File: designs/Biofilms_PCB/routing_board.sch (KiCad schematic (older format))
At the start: 11 parts

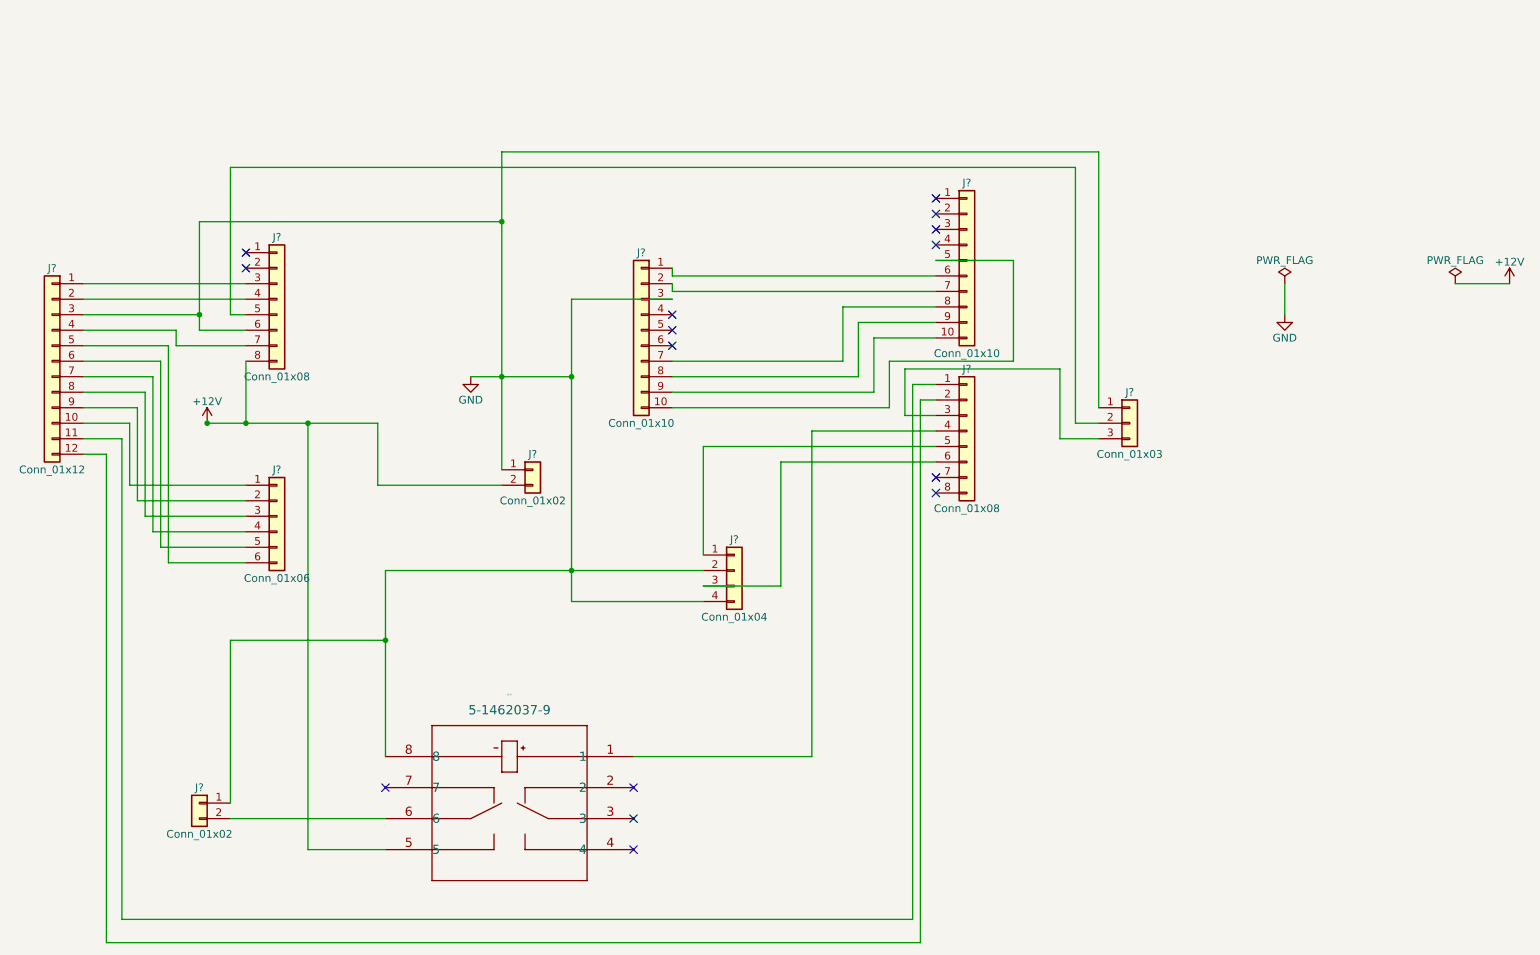
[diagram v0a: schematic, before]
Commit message: drafted v1 of biofilms PCB
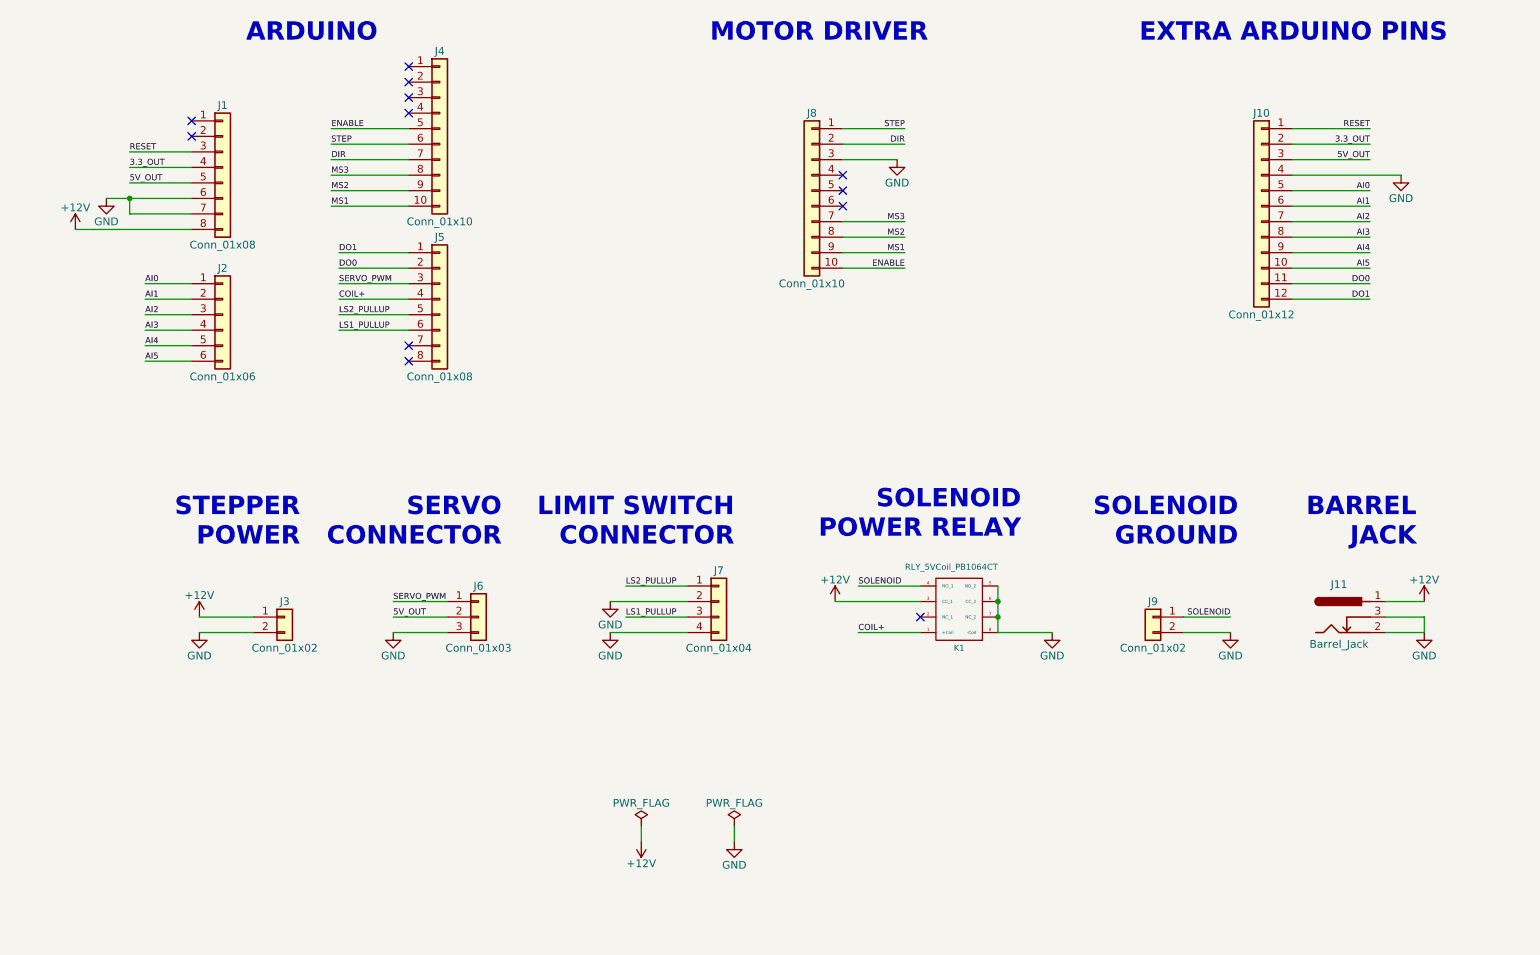
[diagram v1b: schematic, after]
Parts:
- removed RLY?: 5-1462037-9, 5-1462037-9, symbol 5-1462037-9
- added J11: Barrel_Jack, Connectors:BARREL_JACK, symbol Barrel_Jack
- added K1: RLY_5VCoil_PB1064CT, Relays_THT:Relay_DPDT_AXICOM_IMSeries_Pitch3.2mm, symbol RLY_5VCoil_PB1064CT
- J1, J5: renamed from J?; footprint (none) -> Pin_Headers:Pin_Header_Straight_1x08_Pitch2.54mm
- J10: renamed from J?; footprint (none) -> Socket_Strips:Socket_Strip_Straight_1x12_Pitch2.54mm
- J2: renamed from J?; footprint (none) -> Pin_Headers:Pin_Header_Straight_1x06_Pitch2.54mm
- J3, J9: renamed from J?; footprint (none) -> Socket_Strips:Socket_Strip_Straight_1x02_Pitch2.54mm
- J4, J8: renamed from J?; footprint (none) -> Pin_Headers:Pin_Header_Straight_1x10_Pitch2.54mm
- J6: renamed from J?; footprint (none) -> Pin_Headers:Pin_Header_Straight_1x03_Pitch2.54mm
- J7: renamed from J?; footprint (none) -> Socket_Strips:Socket_Strip_Straight_1x04_Pitch2.54mm
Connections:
- net +12V: now also J3.1 (Pin_1), J11.1, K1.3 (CC_1); no longer J3.2 (Pin_2)
- net GND: now also J1.7 (Pin_7), J10.4 (Pin_4), J3.2 (Pin_2), J6.3 (Pin_3), J9.2 (Pin_2), J11.2, J11.3, K1.5 (NO_2), K1.6 (CC_2), K1.7 (NC_2), K1.8 (-Coil); no longer J10.3 (Pin_3), J3.1 (Pin_1), J6.1 (Pin_1), J9.1 (Pin_1)
- net STEP: now reaches J4.6 (Pin_6), J8.1 (Pin_1)
- net ENABLE: now reaches J4.5 (Pin_5), J8.10 (Pin_10)
- net DIR: now reaches J4.7 (Pin_7), J8.2 (Pin_2)
- net MS3: now reaches J4.8 (Pin_8), J8.7 (Pin_7)
- net MS2: now reaches J4.9 (Pin_9), J8.8 (Pin_8)
- net MS1: now reaches J4.10 (Pin_10), J8.9 (Pin_9)
- net DO0: now reaches J10.11 (Pin_11)
- net DO0: now also J5.2 (Pin_2); no longer J5.1 (Pin_1)
- net DO1: now reaches J10.12 (Pin_12)
- net DO1: now also J5.1 (Pin_1); no longer J5.2 (Pin_2)
- net SERVO_PWM: now reaches J5.3 (Pin_3)
- net SERVO_PWM: now also J6.1 (Pin_1); no longer J6.3 (Pin_3)
- net COIL+: now reaches J5.4 (Pin_4)
- net COIL+: now also K1.1 (+Coil)
- net LS2_PULLUP: now reaches J5.5 (Pin_5), J7.1 (Pin_1)
- net LS1_PULLUP: now reaches J5.6 (Pin_6), J7.3 (Pin_3)
- net RESET: now reaches J1.3 (Pin_3), J10.1 (Pin_1)
- net 3.3_OUT: now reaches J1.4 (Pin_4), J10.2 (Pin_2)
- net 5V_OUT: now reaches J1.5 (Pin_5), J6.2 (Pin_2)
- net 5V_OUT: now also J10.3 (Pin_3)
- net AI0: now reaches J2.1 (Pin_1)
- net AI0: now also J10.5 (Pin_5); no longer J10.10 (Pin_10)
- net AI1: now reaches J2.2 (Pin_2)
- net AI1: now also J10.6 (Pin_6); no longer J10.9 (Pin_9)
- net AI2: now reaches J2.3 (Pin_3)
- net AI2: now also J10.7 (Pin_7); no longer J10.8 (Pin_8)
- net AI3: now reaches J2.4 (Pin_4)
- net AI3: now also J10.8 (Pin_8); no longer J10.7 (Pin_7)
- net AI4: now reaches J2.5 (Pin_5)
- net AI4: now also J10.9 (Pin_9); no longer J10.6 (Pin_6)
- net AI5: now reaches J2.6 (Pin_6)
- net AI5: now also J10.10 (Pin_10); no longer J10.5 (Pin_5)
- new net SOLENOID: J9.1 (Pin_1), K1.4 (NO_1)
- no-connect marks 15 -> 12
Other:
- note added: "ARDUINO"
- note added: "BARREL\nJACK"
- note added: "EXTRA ARDUINO PINS\n"
- note added: "LIMIT SWITCH\nCONNECTOR"
- note added: "MOTOR DRIVER"
- note added: "SERVO\nCONNECTOR"
- note added: "SOLENOID\nGROUND"
- note added: "SOLENOID\nPOWER RELAY"
- note added: "STEPPER\nPOWER\n"
- moved on the sheet: J1, J10, J2, J3, J4, J5, J6, J7, J8, J9
